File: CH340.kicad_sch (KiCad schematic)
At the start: 11 parts

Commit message: changed some stuff to ch340 and Lnet B
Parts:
- C? (x3): value (none) -> 100nF; footprint (none) -> Capacitor_SMD:C_0603_1608Metric_Pad1.08x0.95mm_HandSolder
- C?: value (none) -> 10uF
- C? (x2): value (none) -> 22pF; footprint (none) -> Capacitor_SMD:C_0603_1608Metric_Pad1.08x0.95mm_HandSolder
- J?: value (none) -> USB_B_Mini
- R?: value (none) -> 1k; footprint (none) -> Resistor_SMD:R_0603_1608Metric_Pad0.98x0.95mm_HandSolder
- U?: value (none) -> CH340G; footprint (none) -> Package_SO:SOIC-16_3.9x9.9mm_P1.27mm
- Y?: value (none) -> 12MHz; footprint (none) -> custom_kicad_lib_sk:crystal_arduino
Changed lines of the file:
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@@
       (effects (font (size 1.27 1.27)) (justify left))
     )
-    (property "Value" "" (id 1) (at 71.501 88.0622 0)
-      (effects (font (size 1.27 1.27)) (justify left))
-    )
-    (property "Footprint" "" (id 2) (at 69.5452 90.17 0)
+    (property "Value" "100nF" (id 1) (at 71.501 88.0622 0)
+      (effects (font (size 1.27 1.27)) (justify left))
+    )
+    (property "Footprint" "Capacitor_SMD:C_0603_1608Metric_Pad1.08x0.95mm_HandSolder" (id 2) (at 69.5452 90.17 0)
       (effects (font (size 1.27 1.27)) hide)
     )
@@
     (in_bom yes) (on_board yes) (fields_autoplaced)
     (property "Reference" "C?" (id 0) (at 139.7 93.2012 90))
-    (property "Value" "" (id 1) (at 139.7 95.7381 90))
-    (property "Footprint" "" (id 2) (at 143.51 98.0948 0)
+    (property "Value" "100nF" (id 1) (at 139.7 95.7381 90))
+    (property "Footprint" "Capacitor_SMD:C_0603_1608Metric_Pad1.08x0.95mm_HandSolder" (id 2) (at 143.51 98.0948 0)
       (effects (font (size 1.27 1.27)) hide)
     )
@@
       (effects (font (size 1.27 1.27)) hide)
     )
-    (property "Value" "" (id 1) (at 123.19 67.5442 0))
+    (property "Value" "+5V" (id 1) (at 123.19 67.5442 0))
     (property "Footprint" "" (id 2) (at 123.19 71.12 0)
       (effects (font (size 1.27 1.27)) hide)
@@
       (effects (font (size 1.27 1.27)) hide)
     )
-    (property "Value" "" (id 1) (at 106.68 79.3734 0))
+    (property "Value" "GND" (id 1) (at 106.68 79.3734 0))
     (property "Footprint" "" (id 2) (at 106.68 74.93 0)
       (effects (font (size 1.27 1.27)) hide)
@@
       (effects (font (size 1.27 1.27)) (justify left))
     )
-    (property "Value" "" (id 1) (at 50.8 87.63 0)
+    (property "Value" "10uF" (id 1) (at 50.8 87.63 0)
       (effects (font (size 1.27 1.27)) (justify left))
     )
@@
       (effects (font (size 1.27 1.27)) (justify left))
     )
-    (property "Value" "" (id 1) (at 113.411 114.7322 0)
-      (effects (font (size 1.27 1.27)) (justify left))
-    )
-    (property "Footprint" "" (id 2) (at 111.4552 116.84 0)
+    (property "Value" "22pF" (id 1) (at 113.411 114.7322 0)
+      (effects (font (size 1.27 1.27)) (justify left))
+    )
+    (property "Footprint" "Capacitor_SMD:C_0603_1608Metric_Pad1.08x0.95mm_HandSolder" (id 2) (at 111.4552 116.84 0)
       (effects (font (size 1.27 1.27)) hide)
     )
@@
       (effects (font (size 1.27 1.27)) hide)
     )
-    (property "Value" "" (id 1) (at 86.36 122.5534 0))
+    (property "Value" "GND" (id 1) (at 86.36 122.5534 0))
     (property "Footprint" "" (id 2) (at 86.36 118.11 0)
       (effects (font (size 1.27 1.27)) hide)
@@
       (effects (font (size 1.27 1.27)) (justify left))
     )
-    (property "Value" "" (id 1) (at 125.2094 108.7073 0)
-      (effects (font (size 1.27 1.27)) (justify left))
-    )
-    (property "Footprint" "" (id 2) (at 124.46 105.41 0)
+    (property "Value" "CH340G" (id 1) (at 125.2094 108.7073 0)
+      (effects (font (size 1.27 1.27)) (justify left))
+    )
+    (property "Footprint" "Package_SO:SOIC-16_3.9x9.9mm_P1.27mm" (id 2) (at 124.46 105.41 0)
       (effects (font (size 1.27 1.27)) (justify left) hide)
     )
@@
     (in_bom yes) (on_board yes) (fields_autoplaced)
     (property "Reference" "J?" (id 0) (at 87.63 77.5802 0))
-    (property "Value" "" (id 1) (at 87.63 80.1171 0))
+    (property "Value" "USB_B_Mini" (id 1) (at 87.63 80.1171 0))
     (property "Footprint" "" (id 2) (at 91.44 90.17 0)
       (effects (font (size 1.27 1.27)) hide)
@@
     (in_bom yes) (on_board yes) (fields_autoplaced)
     (property "Reference" "C?" (id 0) (at 113.03 67.8012 90))
-    (property "Value" "" (id 1) (at 113.03 70.3381 90))
-    (property "Footprint" "" (id 2) (at 116.84 72.6948 0)
+    (property "Value" "100nF" (id 1) (at 113.03 70.3381 90))
+    (property "Footprint" "Capacitor_SMD:C_0603_1608Metric_Pad1.08x0.95mm_HandSolder" (id 2) (at 116.84 72.6948 0)
       (effects (font (size 1.27 1.27)) hide)
     )
@@
     (in_bom yes) (on_board yes) (fields_autoplaced)
     (property "Reference" "R?" (id 0) (at 138.43 76.5642 90))
-    (property "Value" "" (id 1) (at 138.43 79.1011 90))
-    (property "Footprint" "" (id 2) (at 138.43 83.058 90)
+    (property "Value" "1k" (id 1) (at 138.43 79.1011 90))
+    (property "Footprint" "Resistor_SMD:R_0603_1608Metric_Pad0.98x0.95mm_HandSolder" (id 2) (at 138.43 83.058 90)
       (effects (font (size 1.27 1.27)) hide)
     )
@@
     (in_bom yes) (on_board yes) (fields_autoplaced)
     (property "Reference" "Y?" (id 0) (at 105.41 101.6848 0))
-    (property "Value" "" (id 1) (at 105.41 104.2217 0))
-    (property "Footprint" "" (id 2) (at 105.41 107.95 0)
+    (property "Value" "12MHz" (id 1) (at 105.41 104.2217 0))
+    (property "Footprint" "custom_kicad_lib_sk:crystal_arduino" (id 2) (at 105.41 107.95 0)
       (effects (font (size 1.27 1.27)) hide)
     )
@@
       (effects (font (size 1.27 1.27)) (justify left))
     )
-    (property "Value" "" (id 1) (at 92.71 114.3 0)
-      (effects (font (size 1.27 1.27)) (justify left))
-    )
-    (property "Footprint" "" (id 2) (at 101.2952 116.84 0)
-      (effects (font (size 1.27 1.27)) hide)
-    )
+    (property "Value" "22pF" (id 1) (at 92.71 114.3 0)
+      (effects (font (size 1.27 1.27)) (justify left))
+    )
+    (property "Footprint" "Capacitor_SMD:C_0603_1608Metric_Pad1.08x0.95mm_HandSolder" (id 2) (at 101.2952 116.84 0)
+      (effects (font (size 1.27 1.27)) hide)
+    )

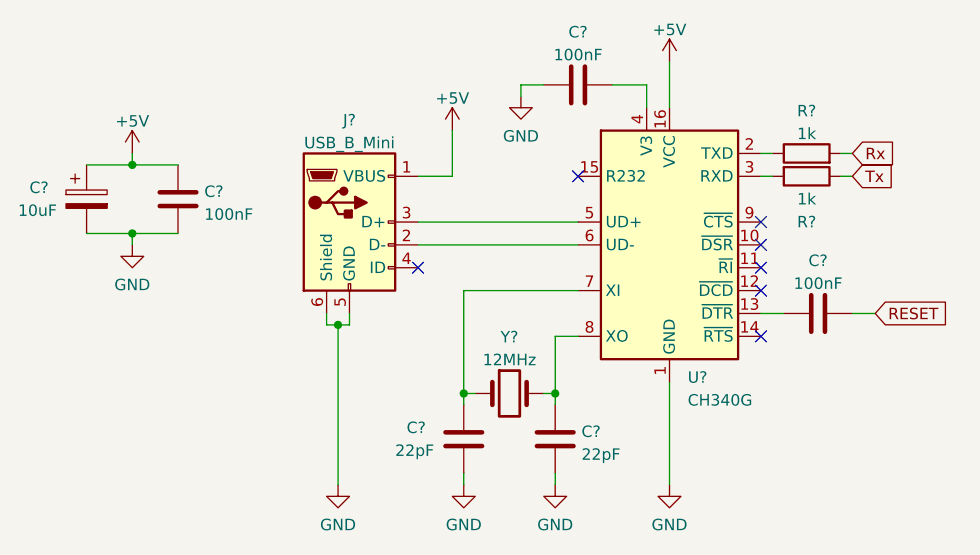
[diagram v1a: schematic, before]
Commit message: added hierarchial labels to some schematics
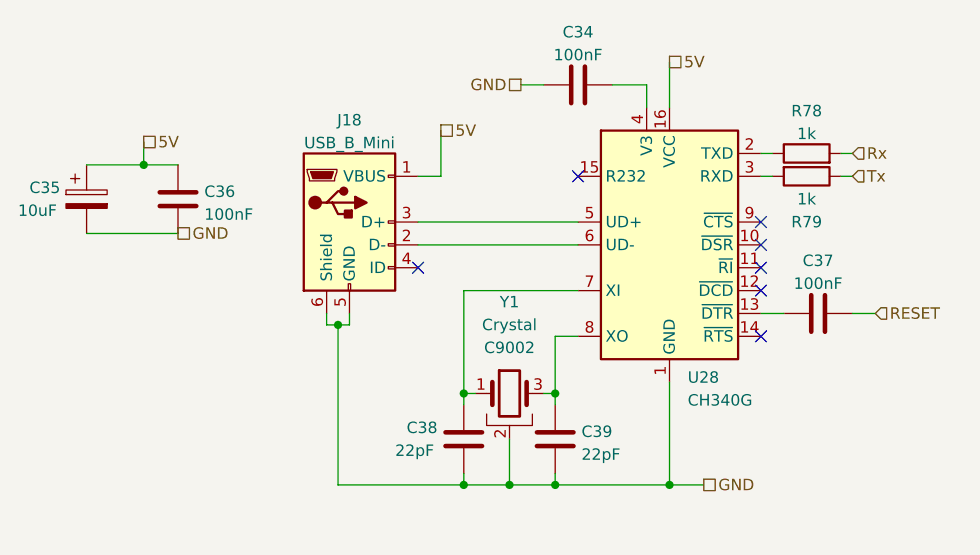
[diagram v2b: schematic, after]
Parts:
- removed Y?: 12MHz, custom_kicad_lib_sk:crystal_arduino, symbol Device:Crystal
- added Y1: Crystal, custom_kicad_lib_sk:crystal_arduino, symbol custom_kicad_lib_sk:crystal_arduino
- gave numbers to parts that had none: 10
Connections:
- net GND: now also Y1.2 (GND), Y1.4 (GND)
- net at C39.1, U28.8 (XO): now also Y1.3
- net at C38.1, U28.7 (XI): now also Y1.1
- net +5V renamed 5V
